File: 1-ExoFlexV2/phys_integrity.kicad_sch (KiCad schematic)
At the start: 23 parts, among them J111 Jumper, J112 Jumper, J113 Jumper, J114 Jumper, J115 Jumper, J116 Jumper, U88 OR Gate, U89 OR Gate, U90 OR Gate, U91 OR Gate, U92 OR Gate

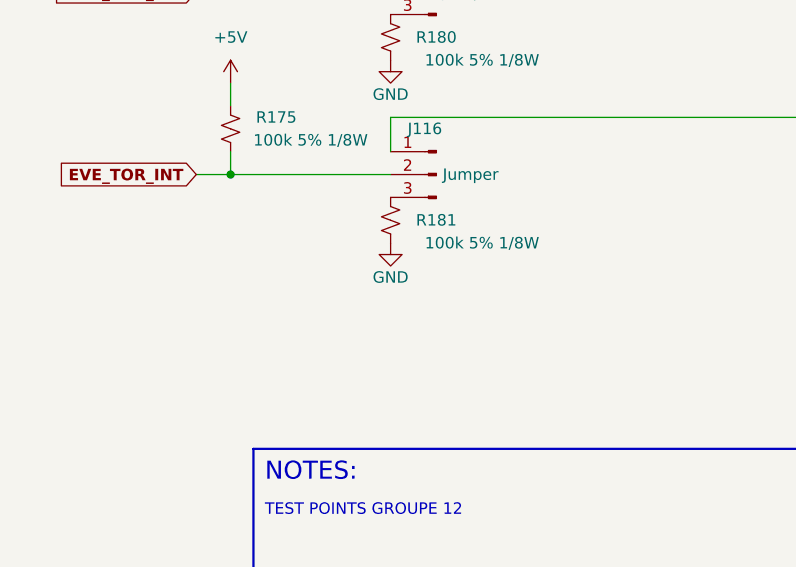
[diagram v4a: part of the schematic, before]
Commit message: Bug NetList
- Ajout de net-tie pour les GND et et les +5V
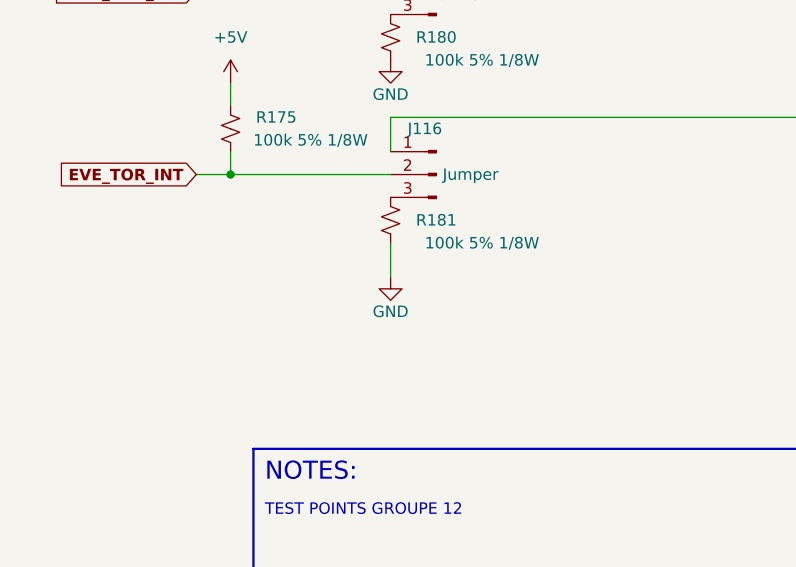
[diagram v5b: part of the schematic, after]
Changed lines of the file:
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@@
+    (stroke (width 0) (type default) (color 0 0 0 0))
+  )
+  (wire (pts (xy 63.5 151.13) (xy 63.5 147.32))
     (stroke (width 0) (type default) (color 0 0 0 0))
   )
@@
   (global_label "DOR_TOR_INT" (shape input) (at 41.91 119.38 180) (fields_autoplaced)
     (effects (font (size 1.27 1.27) (thickness 0.254) bold) (justify right))
-    (property "Intersheet References" "${INTERSHEET_REFS}" (id 0) (at 26.8393 119.507 0)
+    (property "Intersheet References" "${INTERSHEET_REFS}" (id 0) (at 26.8393 119.253 0)
       (effects (font (size 1.27 1.27) (thickness 0.254) bold) (justify right) hide)
     )
@@
   (global_label "EVE_AMP_INT" (shape input) (at 41.91 78.74 180) (fields_autoplaced)
     (effects (font (size 1.27 1.27) (thickness 0.254) bold) (justify right))
-    (property "Intersheet References" "${INTERSHEET_REFS}" (id 0) (at 27.0812 78.867 0)
+    (property "Intersheet References" "${INTERSHEET_REFS}" (id 0) (at 27.0812 78.613 0)
       (effects (font (size 1.27 1.27) (thickness 0.254) bold) (justify right) hide)
     )
@@
   (global_label "EXT_TOR_INT" (shape input) (at 41.91 99.06 180) (fields_autoplaced)
     (effects (font (size 1.27 1.27) (thickness 0.254) bold) (justify right))
-    (property "Intersheet References" "${INTERSHEET_REFS}" (id 0) (at 27.3836 99.187 0)
+    (property "Intersheet References" "${INTERSHEET_REFS}" (id 0) (at 27.3836 98.933 0)
       (effects (font (size 1.27 1.27) (thickness 0.254) bold) (justify right) hide)
     )
@@
   (global_label "DOR_AMP_INT" (shape input) (at 40.64 58.42 180) (fields_autoplaced)
     (effects (font (size 1.27 1.27) (thickness 0.254) bold) (justify right))
-    (property "Intersheet References" "${INTERSHEET_REFS}" (id 0) (at 25.3274 58.547 0)
+    (property "Intersheet References" "${INTERSHEET_REFS}" (id 0) (at 25.3274 58.293 0)
       (effects (font (size 1.27 1.27) (thickness 0.254) bold) (justify right) hide)
     )
@@
   (global_label "EVE_TOR_INT" (shape input) (at 41.91 139.7 180) (fields_autoplaced)
     (effects (font (size 1.27 1.27) (thickness 0.254) bold) (justify right))
-    (property "Intersheet References" "${INTERSHEET_REFS}" (id 0) (at 27.3231 139.827 0)
+    (property "Intersheet References" "${INTERSHEET_REFS}" (id 0) (at 27.3231 139.573 0)
       (effects (font (size 1.27 1.27) (thickness 0.254) bold) (justify right) hide)
     )
@@
   (global_label "EXT_AMP_INT" (shape input) (at 40.64 35.56 180) (fields_autoplaced)
     (effects (font (size 1.27 1.27) (thickness 0.254) bold) (justify right))
-    (property "Intersheet References" "${INTERSHEET_REFS}" (id 0) (at 25.8717 35.687 0)
+    (property "Intersheet References" "${INTERSHEET_REFS}" (id 0) (at 25.8717 35.433 0)
       (effects (font (size 1.27 1.27) (thickness 0.254) bold) (justify right) hide)
     )
@@
   (symbol (lib_id "power:+5V") (at 45.72 109.22 0) (unit 1)
     (in_bom yes) (on_board yes) (fields_autoplaced)
-    (property "Reference" "#PWR0486" (id 0) (at 45.72 113.03 0)
+    (property "Reference" "#PWR0487" (id 0) (at 45.72 113.03 0)
       (effects (font (size 1.27 1.27)) hide)
     )
@@
   (symbol (lib_id "power:+5V") (at 45.72 68.58 0) (unit 1)
     (in_bom yes) (on_board yes) (fields_autoplaced)
-    (property "Reference" "#PWR0484" (id 0) (at 45.72 72.39 0)
+    (property "Reference" "#PWR0485" (id 0) (at 45.72 72.39 0)
       (effects (font (size 1.27 1.27)) hide)
     )
@@
   (symbol (lib_id "power:GND") (at 63.5 86.36 0) (unit 1)
     (in_bom yes) (on_board yes)
-    (property "Reference" "#PWR0490" (id 0) (at 63.5 92.71 0)
+    (property "Reference" "#PWR0491" (id 0) (at 63.5 92.71 0)
       (effects (font (size 1.27 1.27)) hide)
     )
@@
   (symbol (lib_id "power:+5V") (at 45.72 25.4 0) (unit 1)
     (in_bom yes) (on_board yes) (fields_autoplaced)
-    (property "Reference" "#PWR0482" (id 0) (at 45.72 29.21 0)
+    (property "Reference" "#PWR0483" (id 0) (at 45.72 29.21 0)
       (effects (font (size 1.27 1.27)) hide)
     )
@@
   (symbol (lib_id "power:GND") (at 146.05 55.88 0) (unit 1)
     (in_bom yes) (on_board yes) (fields_autoplaced)
-    (property "Reference" "#PWR0497" (id 0) (at 146.05 62.23 0)
+    (property "Reference" "#PWR0498" (id 0) (at 146.05 62.23 0)
       (effects (font (size 1.27 1.27)) hide)
     )
@@
   (symbol (lib_id "power:+5V") (at 144.78 85.09 0) (unit 1)
     (in_bom yes) (on_board yes) (fields_autoplaced)
-    (property "Reference" "#PWR0494" (id 0) (at 144.78 88.9 0)
+    (property "Reference" "#PWR0495" (id 0) (at 144.78 88.9 0)
       (effects (font (size 1.27 1.27)) hide)
     )
@@
   (symbol (lib_id "power:+5V") (at 191.77 116.84 0) (unit 1)
     (in_bom yes) (on_board yes) (fields_autoplaced)
-    (property "Reference" "#PWR0498" (id 0) (at 191.77 120.65 0)
+    (property "Reference" "#PWR0499" (id 0) (at 191.77 120.65 0)
       (effects (font (size 1.27 1.27)) hide)
     )
@@
   (symbol (lib_id "power:GND") (at 191.77 138.43 0) (unit 1)
     (in_bom yes) (on_board yes) (fields_autoplaced)
-    (property "Reference" "#PWR0499" (id 0) (at 191.77 144.78 0)
+    (property "Reference" "#PWR0500" (id 0) (at 191.77 144.78 0)
       (effects (font (size 1.27 1.27)) hide)
     )
@@
   (symbol (lib_id "power:GND") (at 63.5 66.04 0) (unit 1)
     (in_bom yes) (on_board yes)
-    (property "Reference" "#PWR0489" (id 0) (at 63.5 72.39 0)
+    (property "Reference" "#PWR0490" (id 0) (at 63.5 72.39 0)
       (effects (font (size 1.27 1.27)) hide)
     )
@@
   (symbol (lib_id "power:+5V") (at 45.72 129.54 0) (unit 1)
     (in_bom yes) (on_board yes) (fields_autoplaced)
-    (property "Reference" "#PWR0487" (id 0) (at 45.72 133.35 0)
+    (property "Reference" "#PWR0488" (id 0) (at 45.72 133.35 0)
       (effects (font (size 1.27 1.27)) hide)
     )
@@
   (symbol (lib_id "power:GND") (at 63.5 127 0) (unit 1)
     (in_bom yes) (on_board yes)
-    (property "Reference" "#PWR0492" (id 0) (at 63.5 133.35 0)
+    (property "Reference" "#PWR0493" (id 0) (at 63.5 133.35 0)
       (effects (font (size 1.27 1.27)) hide)
     )
@@
   (symbol (lib_id "power:GND") (at 193.04 67.31 0) (unit 1)
     (in_bom yes) (on_board yes) (fields_autoplaced)
-    (property "Reference" "#PWR0501" (id 0) (at 193.04 73.66 0)
+    (property "Reference" "#PWR0502" (id 0) (at 193.04 73.66 0)
       (effects (font (size 1.27 1.27)) hide)
     )
@@
   (symbol (lib_id "power:+5V") (at 193.04 46.99 0) (unit 1)
     (in_bom yes) (on_board yes) (fields_autoplaced)
-    (property "Reference" "#PWR0500" (id 0) (at 193.04 50.8 0)
+    (property "Reference" "#PWR0501" (id 0) (at 193.04 50.8 0)
       (effects (font (size 1.27 1.27)) hide)
     )
@@
   (symbol (lib_id "power:GND") (at 63.5 106.68 0) (unit 1)
     (in_bom yes) (on_board yes)
-    (property "Reference" "#PWR0491" (id 0) (at 63.5 113.03 0)
+    (property "Reference" "#PWR0492" (id 0) (at 63.5 113.03 0)
       (effects (font (size 1.27 1.27)) hide)
     )
@@
   (symbol (lib_id "power:GND") (at 63.5 43.18 0) (unit 1)
     (in_bom yes) (on_board yes)
-    (property "Reference" "#PWR0488" (id 0) (at 63.5 49.53 0)
+    (property "Reference" "#PWR0489" (id 0) (at 63.5 49.53 0)
       (effects (font (size 1.27 1.27)) hide)
     )
@@
     (pin "3")
   )
-  (symbol (lib_id "power:GND") (at 63.5 147.32 0) (unit 1)
-    (in_bom yes) (on_board yes)
-    (property "Reference" "#PWR0493" (id 0) (at 63.5 153.67 0)
-      (effects (font (size 1.27 1.27)) hide)
-    )
-    (property "Value" "GND" (id 1) (at 63.5 151.13 0))
-    (property "Footprint" "" (id 2) (at 63.5 147.32 0)
-      (effects (font (size 1.27 1.27)) hide)
-    )
-    (property "Datasheet" "" (id 3) (at 63.5 147.32 0)
+  (symbol (lib_id "power:GND") (at 63.5 151.13 0) (unit 1)
+    (in_bom yes) (on_board yes)
+    (property "Reference" "#PWR0494" (id 0) (at 63.5 157.48 0)
+      (effects (font (size 1.27 1.27)) hide)
+    )
+    (property "Value" "GND" (id 1) (at 63.5 154.94 0))
+    (property "Footprint" "" (id 2) (at 63.5 151.13 0)
+      (effects (font (size 1.27 1.27)) hide)
+    )
+    (property "Datasheet" "" (id 3) (at 63.5 151.13 0)
       (effects (font (size 1.27 1.27)) hide)
     )
@@
   (symbol (lib_id "power:GND") (at 144.78 105.41 0) (unit 1)
     (in_bom yes) (on_board yes) (fields_autoplaced)
-    (property "Reference" "#PWR0495" (id 0) (at 144.78 111.76 0)
+    (property "Reference" "#PWR0496" (id 0) (at 144.78 111.76 0)
       (effects (font (size 1.27 1.27)) hide)
     )
@@
   (symbol (lib_id "power:GND") (at 234.95 104.14 0) (unit 1)
     (in_bom yes) (on_board yes) (fields_autoplaced)
-    (property "Reference" "#PWR0503" (id 0) (at 234.95 110.49 0)
+    (property "Reference" "#PWR0504" (id 0) (at 234.95 110.49 0)
       (effects (font (size 1.27 1.27)) hide)
     )
@@
   (symbol (lib_id "power:+5V") (at 234.95 82.55 0) (unit 1)
     (in_bom yes) (on_board yes) (fields_autoplaced)
-    (property "Reference" "#PWR0502" (id 0) (at 234.95 86.36 0)
+    (property "Reference" "#PWR0503" (id 0) (at 234.95 86.36 0)
       (effects (font (size 1.27 1.27)) hide)
     )
@@
   (symbol (lib_id "power:+5V") (at 45.72 48.26 0) (unit 1)
     (in_bom yes) (on_board yes) (fields_autoplaced)
-    (property "Reference" "#PWR0483" (id 0) (at 45.72 52.07 0)
+    (property "Reference" "#PWR0484" (id 0) (at 45.72 52.07 0)
       (effects (font (size 1.27 1.27)) hide)
     )
@@
   (symbol (lib_id "power:+5V") (at 45.72 88.9 0) (unit 1)
     (in_bom yes) (on_board yes) (fields_autoplaced)
-    (property "Reference" "#PWR0485" (id 0) (at 45.72 92.71 0)
+    (property "Reference" "#PWR0486" (id 0) (at 45.72 92.71 0)
       (effects (font (size 1.27 1.27)) hide)
     )
@@
   (symbol (lib_id "power:+5V") (at 146.05 36.83 0) (unit 1)
     (in_bom yes) (on_board yes) (fields_autoplaced)
-    (property "Reference" "#PWR0496" (id 0) (at 146.05 40.64 0)
-      (effects (font (size 1.27 1.27)) hide)
-    )
+    (property "Reference" "#PWR0497" (id 0) (at 146.05 40.64 0)
+      (effects (font (size 1.27 1.27)) hide)
+    )

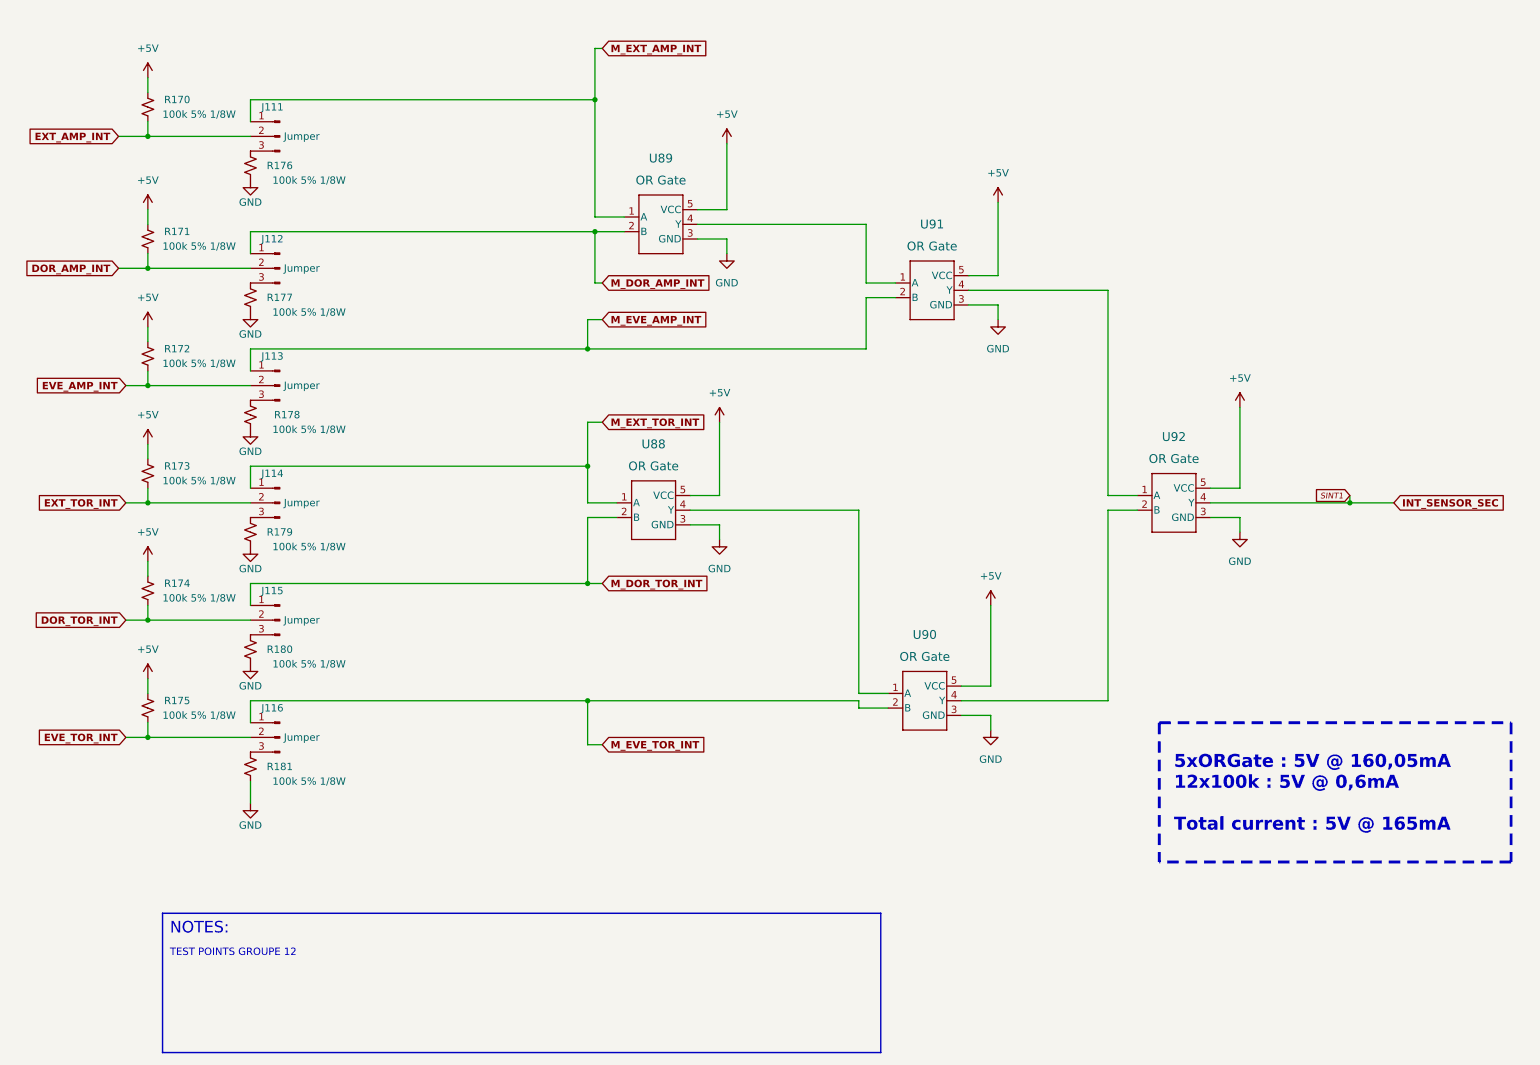
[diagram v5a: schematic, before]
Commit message: Finalisation 3
- Changement des régulateur de tension
- Retrait de test point inutile
- Changement de jumper mal positionner
- Ajout de Mounting holes et fiducial
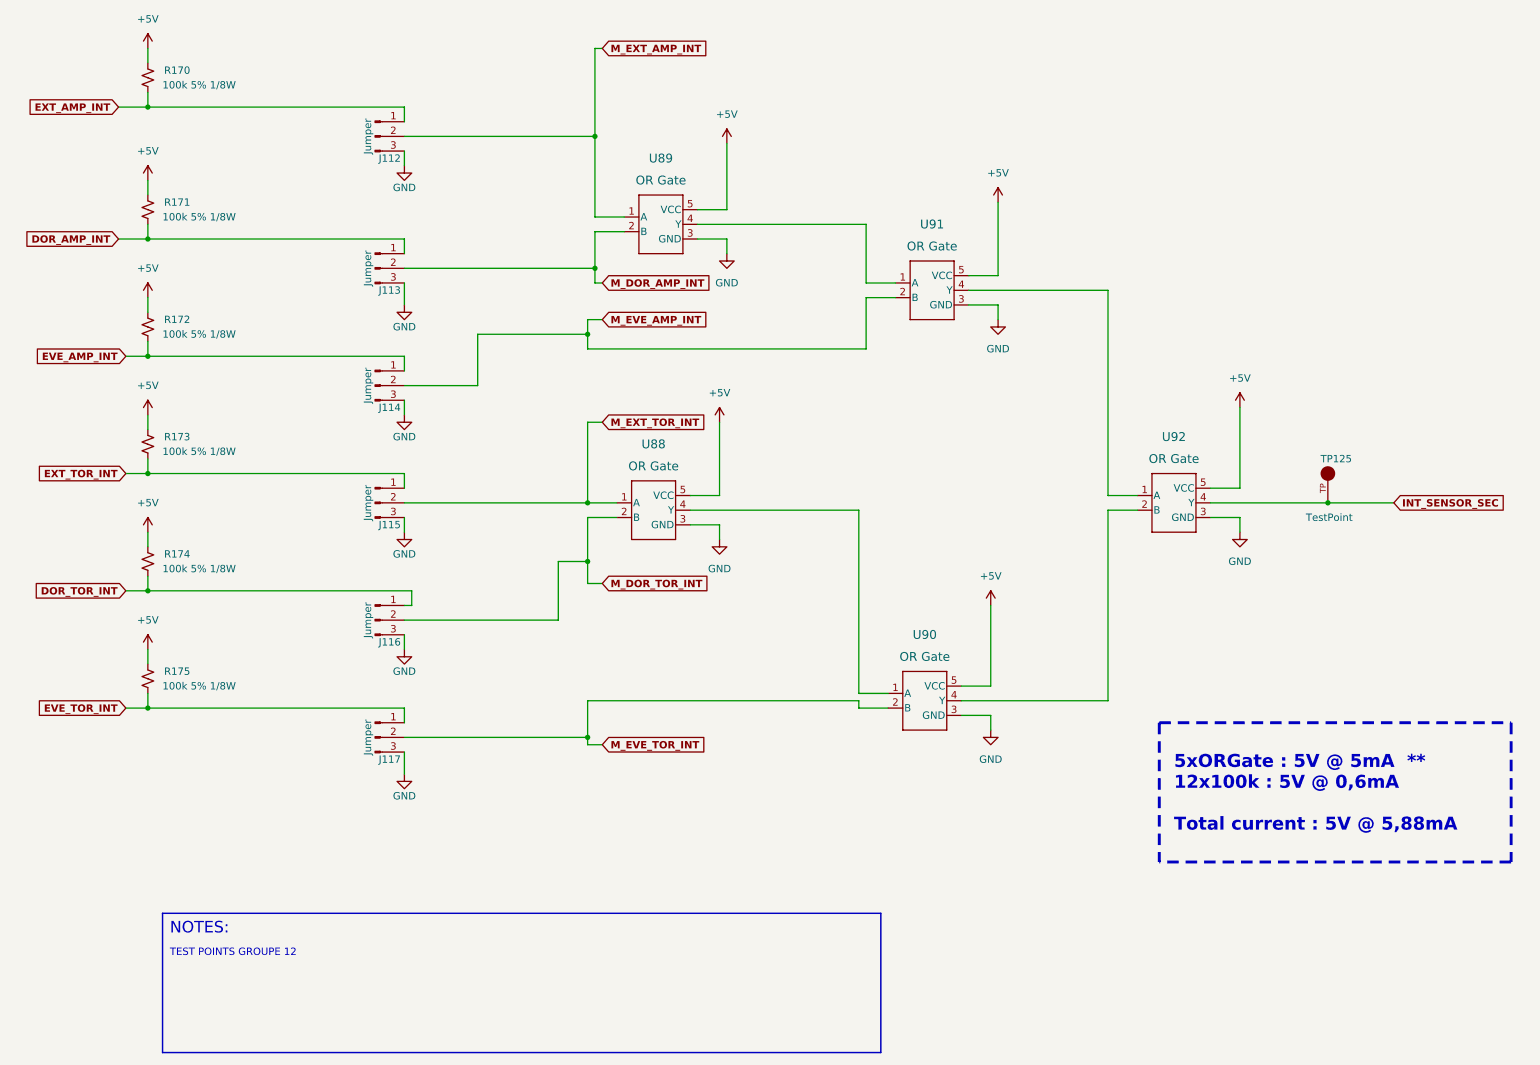
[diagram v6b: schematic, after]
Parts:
- removed R176, R177, R178, R179, R180, R181: 100k 5% 1/8W, Resistor_SMD:R_0805_2012Metric, symbol Device:R_Small_US
- added TP125: TestPoint, FootPrint:KEYSTONE_5005, symbol SymLib:5005
- J112: renamed from J111; footprint Connector_PinSocket_2.54mm:PinSocket_1x03_P2.54mm_Vertical -> Connector_PinHeader_2.54mm:PinHeader_1x03_P2.54mm_Vertical
- J113: renamed from J112; footprint Connector_PinSocket_2.54mm:PinSocket_1x03_P2.54mm_Vertical -> Connector_PinHeader_2.54mm:PinHeader_1x03_P2.54mm_Vertical
- J114: renamed from J113; footprint Connector_PinSocket_2.54mm:PinSocket_1x03_P2.54mm_Vertical -> Connector_PinHeader_2.54mm:PinHeader_1x03_P2.54mm_Vertical
- J115: renamed from J114; footprint Connector_PinSocket_2.54mm:PinSocket_1x03_P2.54mm_Vertical -> Connector_PinHeader_2.54mm:PinHeader_1x03_P2.54mm_Vertical
- J116: renamed from J115; footprint Connector_PinSocket_2.54mm:PinSocket_1x03_P2.54mm_Vertical -> Connector_PinHeader_2.54mm:PinHeader_1x03_P2.54mm_Vertical
- J117: renamed from J116; footprint Connector_PinSocket_2.54mm:PinSocket_1x03_P2.54mm_Vertical -> Connector_PinHeader_2.54mm:PinHeader_1x03_P2.54mm_Vertical
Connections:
- net DOR_AMP_INT: now also J113.1 (Pin_1); no longer J113.2 (Pin_2)
- net DOR_TOR_INT: now also J116.1 (Pin_1); no longer J116.2 (Pin_2)
- net EVE_AMP_INT: now also J114.1 (Pin_1); no longer J114.2 (Pin_2)
- net EVE_TOR_INT: now also J117.1 (Pin_1); no longer J117.2 (Pin_2)
- net EXT_AMP_INT: now also J112.1 (Pin_1); no longer J112.2 (Pin_2)
- net EXT_TOR_INT: now also J115.1 (Pin_1); no longer J115.2 (Pin_2)
- net GND: now also J112.3 (Pin_3), J113.3 (Pin_3), J114.3 (Pin_3), J115.3 (Pin_3), J116.3 (Pin_3), J117.3 (Pin_3)
- net INT_SENSOR_SEC: now also TP125.TP
- net M_DOR_AMP_INT: now also J113.2 (Pin_2); no longer J113.1 (Pin_1)
- net M_DOR_TOR_INT: now also J116.2 (Pin_2); no longer J116.1 (Pin_1)
- net M_EVE_AMP_INT: now also J114.2 (Pin_2); no longer J114.1 (Pin_1)
- net M_EVE_TOR_INT: now also J117.2 (Pin_2); no longer J117.1 (Pin_1)
- net M_EXT_AMP_INT: now also J112.2 (Pin_2); no longer J112.1 (Pin_1)
- net M_EXT_TOR_INT: now also J115.2 (Pin_2); no longer J115.1 (Pin_1)
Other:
- note added: "5xORGate : 5V @ 5mA ** 12x100k : 5V @ 0,6mA Total current : 5V @ 5,88mA"
- note removed: "5xORGate : 5V @ 160,05mA 12x100k : 5V @ 0,6mA Total current : 5V @ 165mA"
- moved on the sheet: J112, J113, J114, J115, J116, J117, R170, R171, R172, R173, R174, R175
